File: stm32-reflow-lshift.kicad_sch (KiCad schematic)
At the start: 16 parts, among them J6 Conn_02x08_Odd_Even, Q1 2N7002, Q10 2N7002, Q11 2N7002, Q3 2N7002, Q4 2N7002, Q5 2N7002, Q6 2N7002, Q7 2N7002, Q8 2N7002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

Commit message: organized schematic more, fixed net naming of rw
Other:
- note added: "R/~{W}"
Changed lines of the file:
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@@
   (junction (at 167.64 86.36) (diameter 0) (color 0 0 0 0))
   (junction (at 167.64 99.06) (diameter 0) (color 0 0 0 0))
-  (junction (at 173.99 54.61) (diameter 0) (color 0 0 0 0))
   (junction (at 193.04 86.36) (diameter 0) (color 0 0 0 0))
   (junction (at 193.04 99.06) (diameter 0) (color 0 0 0 0))
@@
     (stroke (width 0) (type default) (color 0 0 0 0))
   )
-  (wire (pts (xy 148.59 54.61) (xy 173.99 54.61))
+  (wire (pts (xy 148.59 54.61) (xy 199.39 54.61))
     (stroke (width 0) (type default) (color 0 0 0 0))
   )
@@
     (stroke (width 0) (type default) (color 0 0 0 0))
   )
-  (wire (pts (xy 173.99 41.7435) (xy 173.99 54.61))
-    (stroke (width 0) (type default) (color 0 0 0 0))
-  )
-  (wire (pts (xy 173.99 41.7435) (xy 185.42 41.7435))
-    (stroke (width 0) (type default) (color 0 0 0 0))
-  )
-  (wire (pts (xy 173.99 54.61) (xy 199.39 54.61))
-    (stroke (width 0) (type default) (color 0 0 0 0))
-  )
   (wire (pts (xy 179.07 92.71) (xy 185.42 92.71))
     (stroke (width 0) (type default) (color 0 0 0 0))
@@
   )
   (polyline (pts (xy 151.765 194.945) (xy 151.765 198.12))
+    (stroke (width 0) (type default) (color 0 0 0 0))
+  )
+  (polyline (pts (xy 172.72 41.91) (xy 185.42 41.91))
+    (stroke (width 0) (type default) (color 0 0 0 0))
+  )
+  (polyline (pts (xy 172.72 54.61) (xy 172.72 41.91))
     (stroke (width 0) (type default) (color 0 0 0 0))
   )
@@
     (effects (font (size 1.27 1.27)) (justify right bottom))
   )
+  (text "R/~{W}" (at 96.52 171.45 0)
+    (effects (font (size 1.27 1.27) italic) (justify left bottom))
+  )
   (text "WRITE-ONLY" (at 172.72 48.26 180)
     (effects (font (size 1.27 1.27) italic) (justify right bottom))
@@
     (effects (font (size 1.27 1.27)) (justify right bottom))
   )
+  (text "R/~{W}" (at 185.42 41.91 180)
+    (effects (font (size 1.27 1.27) italic) (justify right bottom))
+  )
   (text "Level Shifting FETs" (at 284.48 113.665 180)
     (effects (font (size 1.27 1.27)) (justify right bottom))
@@
     (effects (font (size 1.27 1.27)) (justify left bottom))
   )
-  (label "LR{slash}~{W}" (at 96.52 171.45 0)
-    (effects (font (size 1.27 1.27)) (justify left bottom))
-  )
   (label "LDB0" (at 96.52 173.99 0)
     (effects (font (size 1.27 1.27)) (justify left bottom))
@@
   (label "DB4" (at 179.07 92.71 0)
     (effects (font (size 1.27 1.27)) (justify left bottom))
-  )
-  (label "LR{slash}~{W}" (at 185.42 41.7435 180)
-    (effects (font (size 1.27 1.27)) (justify right bottom))
   )
   (label "E" (at 185.42 48.26 0)
@@
     (pin "1")
   )
+  (symbol (lib_id "power:GND") (at 96.52 171.45 270) (unit 1)
+    (in_bom yes) (on_board yes) (fields_autoplaced)
+    (property "Reference" "#PWR0103" (id 0) (at 90.17 171.45 0)
+      (effects (font (size 1.27 1.27)) hide)
+    )
+    (property "Value" "GND" (id 1) (at 93.345 171.929 90)
+      (effects (font (size 1.27 1.27)) (justify right))
+    )
+    (property "Footprint" "" (id 2) (at 96.52 171.45 0)
+      (effects (font (size 1.27 1.27)) hide)
+    )
+    (property "Datasheet" "" (id 3) (at 96.52 171.45 0)
+      (effects (font (size 1.27 1.27)) hide)
+    )
+    (pin "1")
+  )
   (symbol (lib_id "power:GND") (at 199.39 55.88 0) (unit 1)
     (in_bom yes) (on_board yes) (fields_autoplaced)
@@
     (pin "3")
   )
-  (symbol (lib_name "2N7002_4") (lib_id "Transistor_FET:2N7002") (at 114.3 92.71 0) (unit 1)
+  (symbol (lib_id "Transistor_FET:2N7002") (at 114.3 92.71 0) (unit 1)
     (in_bom yes) (on_board yes)
     (property "Reference" "Q5" (id 0) (at 119.5324 91.8015 0)
@@
     (pin "3")
   )
-  (symbol (lib_name "2N7002_3") (lib_id "Transistor_FET:2N7002") (at 139.7 92.71 0) (unit 1)
+  (symbol (lib_id "Transistor_FET:2N7002") (at 139.7 92.71 0) (unit 1)
     (in_bom yes) (on_board yes)
     (property "Reference" "Q6" (id 0) (at 144.9324 91.8015 0)
@@
     (pin "3")
   )
-  (symbol (lib_name "2N7002_7") (lib_id "Transistor_FET:2N7002") (at 146.05 48.26 0) (unit 1)
+  (symbol (lib_id "Transistor_FET:2N7002") (at 146.05 48.26 0) (unit 1)
     (in_bom yes) (on_board yes) (fields_autoplaced)
     (property "Reference" "Q1" (id 0) (at 151.2824 47.3515 0)
@@
     (pin "3")
   )
-  (symbol (lib_name "2N7002_6") (lib_id "Transistor_FET:2N7002") (at 165.1 92.71 0) (unit 1)
+  (symbol (lib_id "Transistor_FET:2N7002") (at 165.1 92.71 0) (unit 1)
     (in_bom yes) (on_board yes) (fields_autoplaced)
     (property "Reference" "Q7" (id 0) (at 170.3324 91.8015 0)
@@
     (pin "3")
   )
-  (symbol (lib_name "2N7002_2") (lib_id "Transistor_FET:2N7002") (at 196.85 48.26 0) (unit 1)
+  (symbol (lib_id "Transistor_FET:2N7002") (at 196.85 48.26 0) (unit 1)
     (in_bom yes) (on_board yes) (fields_autoplaced)
     (property "Reference" "Q3" (id 0) (at 202.0824 47.3515 0)
@@
     (pin "3")
   )
-  (symbol (lib_name "2N7002_9") (lib_id "Transistor_FET:2N7002") (at 215.9 92.71 0) (unit 1)
+  (symbol (lib_id "Transistor_FET:2N7002") (at 215.9 92.71 0) (unit 1)
     (in_bom yes) (on_board yes) (fields_autoplaced)
     (property "Reference" "Q9" (id 0) (at 221.1324 91.8015 0)
@@
     (pin "3")
   )
-  (symbol (lib_name "2N7002_10") (lib_id "Transistor_FET:2N7002") (at 241.3 92.71 0) (unit 1)
+  (symbol (lib_id "Transistor_FET:2N7002") (at 241.3 92.71 0) (unit 1)
     (in_bom yes) (on_board yes) (fields_autoplaced)
     (property "Reference" "Q10" (id 0) (at 246.5324 91.8015 0)
@@
     (pin "3")
   )
-  (symbol (lib_name "2N7002_8") (lib_id "Transistor_FET:2N7002") (at 266.7 92.71 0) (unit 1)
+  (symbol (lib_id "Transistor_FET:2N7002") (at 266.7 92.71 0) (unit 1)
     (in_bom yes) (on_board yes) (fields_autoplaced)
     (property "Reference" "Q11" (id 0) (at 271.9324 91.8015 0)

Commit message: updated bom to reflect non-backordered parts
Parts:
- J6: DigiKey Part # (none) -> S9171-ND
- Q1, Q10, Q11, Q3, Q4, Q5, Q6, Q7, Q8, Q9: DigiKey Part # (none) -> 1727-8642-1-ND
- R2: DigiKey Part # (none) -> RMCF0805JT33R0CT-ND
- RN1, RN2: DigiKey Part # (none) -> 4611X-101-103LF-ND
- RV1: DigiKey Part # (none) -> ST4ETB103CT-ND
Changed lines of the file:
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@@
+      (effects (font (size 1.27 1.27)) hide)
+    )
+    (property "DigiKey Part #" "RMCF0805JT33R0CT-ND" (id 4) (at 31.75 31.75 0)
       (effects (font (size 1.27 1.27)) hide)
     )
@@
       (effects (font (size 1.27 1.27)) hide)
     )
+    (property "DigiKey Part #" "ST4ETB103CT-ND" (id 4) (at 31.75 55.88 0)
+      (effects (font (size 1.27 1.27)) hide)
+    )
     (pin "1")
     (pin "2")
@@
     (property "Datasheet" "https://www.fairchildsemi.com/datasheets/2N/2N7002.pdf" (id 3) (at 88.9 92.71 0)
       (effects (font (size 1.27 1.27)) (justify left) hide)
+    )
+    (property "DigiKey Part #" "1727-8642-1-ND" (id 4) (at 88.9 92.71 0)
+      (effects (font (size 1.27 1.27)) hide)
     )
     (pin "1")
@@
       (effects (font (size 1.27 1.27)) (justify left) hide)
     )
+    (property "DigiKey Part #" "1727-8642-1-ND" (id 4) (at 114.3 92.71 0)
+      (effects (font (size 1.27 1.27)) hide)
+    )
     (pin "1")
     (pin "2")
@@
       (effects (font (size 1.27 1.27)) (justify left) hide)
     )
+    (property "DigiKey Part #" "1727-8642-1-ND" (id 4) (at 139.7 92.71 0)
+      (effects (font (size 1.27 1.27)) hide)
+    )
     (pin "1")
     (pin "2")
@@
       (effects (font (size 1.27 1.27)) (justify left) hide)
     )
+    (property "DigiKey Part #" "1727-8642-1-ND" (id 4) (at 146.05 48.26 0)
+      (effects (font (size 1.27 1.27)) hide)
+    )
     (pin "1")
     (pin "2")
@@
       (effects (font (size 1.27 1.27)) (justify left) hide)
     )
+    (property "DigiKey Part #" "1727-8642-1-ND" (id 4) (at 165.1 92.71 0)
+      (effects (font (size 1.27 1.27)) hide)
+    )
     (pin "1")
     (pin "2")
@@
       (effects (font (size 1.27 1.27)) (justify left) hide)
     )
+    (property "DigiKey Part #" "1727-8642-1-ND" (id 4) (at 190.5 92.71 0)
+      (effects (font (size 1.27 1.27)) hide)
+    )
     (pin "1")
     (pin "2")
@@
       (effects (font (size 1.27 1.27)) (justify left) hide)
     )
+    (property "DigiKey Part #" "1727-8642-1-ND" (id 4) (at 196.85 48.26 0)
+      (effects (font (size 1.27 1.27)) hide)
+    )
     (pin "1")
     (pin "2")
@@
       (effects (font (size 1.27 1.27)) (justify left) hide)
     )
+    (property "DigiKey Part #" "1727-8642-1-ND" (id 4) (at 215.9 92.71 0)
+      (effects (font (size 1.27 1.27)) hide)
+    )
     (pin "1")
     (pin "2")
@@
       (effects (font (size 1.27 1.27)) (justify left) hide)
     )
+    (property "DigiKey Part #" "1727-8642-1-ND" (id 4) (at 241.3 92.71 0)
+      (effects (font (size 1.27 1.27)) hide)
+    )
     (pin "1")
     (pin "2")
@@
     (property "Datasheet" "https://www.fairchildsemi.com/datasheets/2N/2N7002.pdf" (id 3) (at 266.7 92.71 0)
       (effects (font (size 1.27 1.27)) (justify left) hide)
+    )
+    (property "DigiKey Part #" "1727-8642-1-ND" (id 4) (at 266.7 92.71 0)
+      (effects (font (size 1.27 1.27)) hide)
     )
     (pin "1")
@@
     )
     (property "Datasheet" "http://www.vishay.com/docs/31509/csc.pdf" (id 3) (at 60.96 173.99 0)
+      (effects (font (size 1.27 1.27)) hide)
+    )
+    (property "DigiKey Part #" "4611X-101-103LF-ND" (id 4) (at 60.96 173.99 0)
       (effects (font (size 1.27 1.27)) hide)
     )
@@
       (effects (font (size 1.27 1.27)) hide)
     )
+    (property "DigiKey Part #" "4611X-101-103LF-ND" (id 4) (at 104.14 26.67 0)
+      (effects (font (size 1.27 1.27)) hide)
+    )
     (pin "1")
     (pin "10")
@@
       (effects (font (size 1.27 1.27)) hide)
     )
+    (property "DigiKey Part #" "S9171-ND" (id 4) (at 110.49 171.45 0)
+      (effects (font (size 1.27 1.27)) hide)
+    )

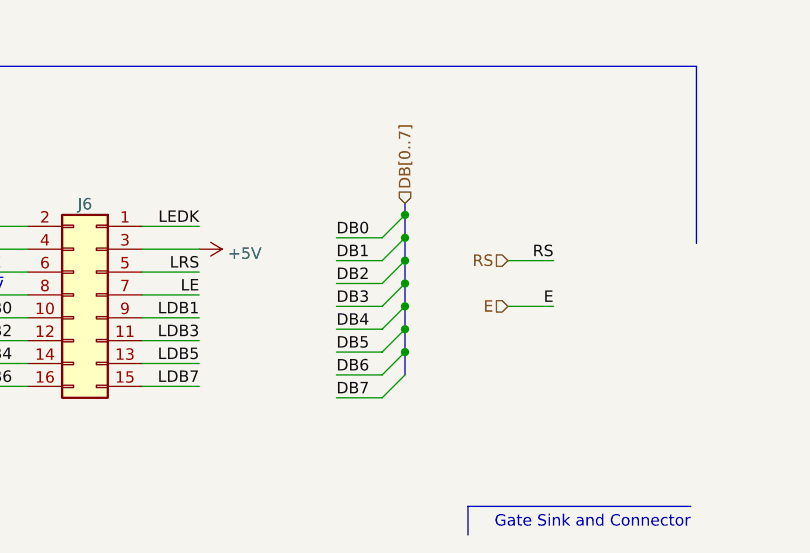
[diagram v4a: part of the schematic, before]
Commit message: updated board for proper kicad6.0 compati
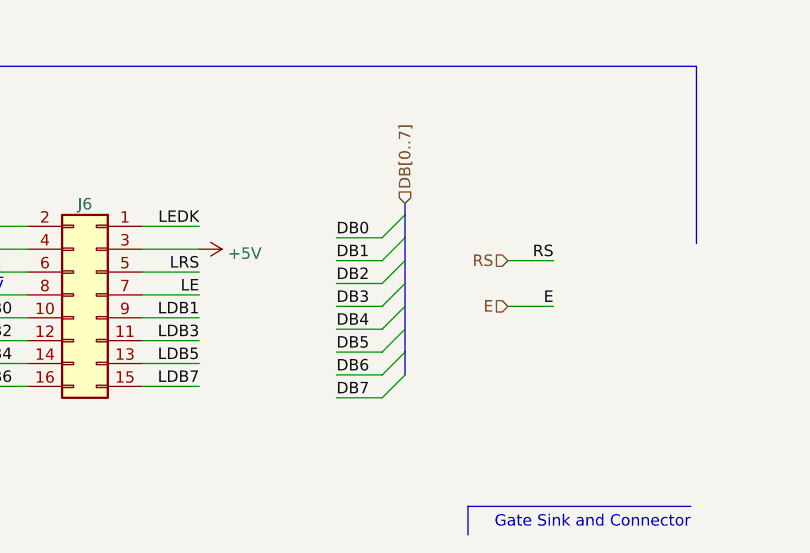
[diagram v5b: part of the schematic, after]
